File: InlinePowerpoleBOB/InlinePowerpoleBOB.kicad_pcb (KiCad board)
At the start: 2 copper layers, 65.4 x 36.8 mm, 17 parts, among them IC1 LTC4368IMS-2#PBF, Q1 DMT6002LPS-13, Q2 DMT6002LPS-13

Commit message: PCB Updates
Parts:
- added G***: LOGO, OpenSourceLogos:ohs-logo, B.Cu at (128.5, 60.5)
- J1: renamed from Input; footprint SamacSys_Parts:Anderson_powerpole_2w -> SamacSys_Parts:Anderson_powerpole_2w_90
- J2: renamed from Output; footprint SamacSys_Parts:Anderson_powerpole_2w -> SamacSys_Parts:Anderson_powerpole_2w_90
- moved J1 2.79 mm to (117.1, 55.2)
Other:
- board text added: "Inline Poerpole protection by Gareth Blades M7GRB Based on the design by Bernard McIntosh GM4WZG featured in RadCom September 2021"
- board text added: "Input"
- board text added: "Output"
- board text added: "https://bit.ly/2YlUq2V"

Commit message: Fixed PCB text
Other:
- board text added: "Inline Powerpole protection by Gareth Blades M7GRB Based on the design by Bernard McIntosh GM4WZG featured in RadCom September 2021"
- board text removed: "Inline Poerpole protection by Gareth Blades M7GRB Based on the design by Bernard McIntosh GM4WZG featured in RadCom September 2021"

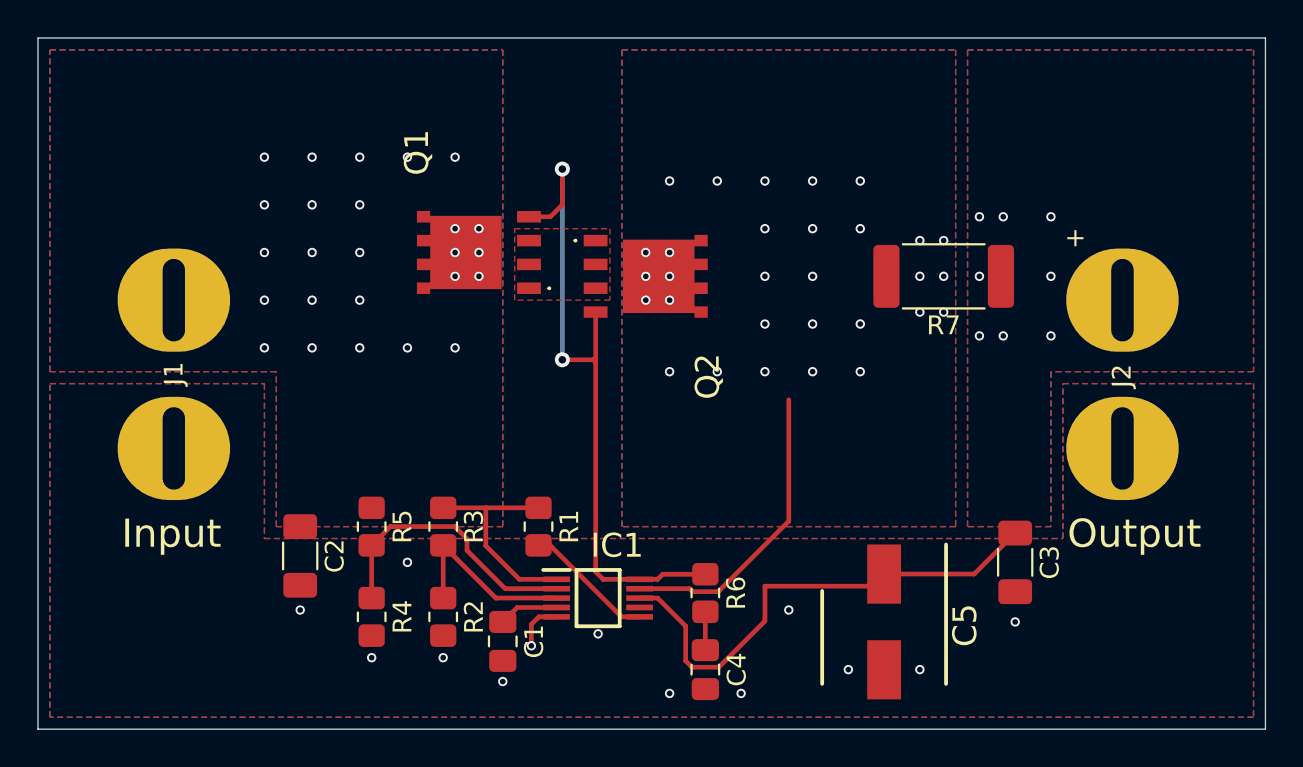
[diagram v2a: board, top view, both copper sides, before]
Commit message: Removed over current feature
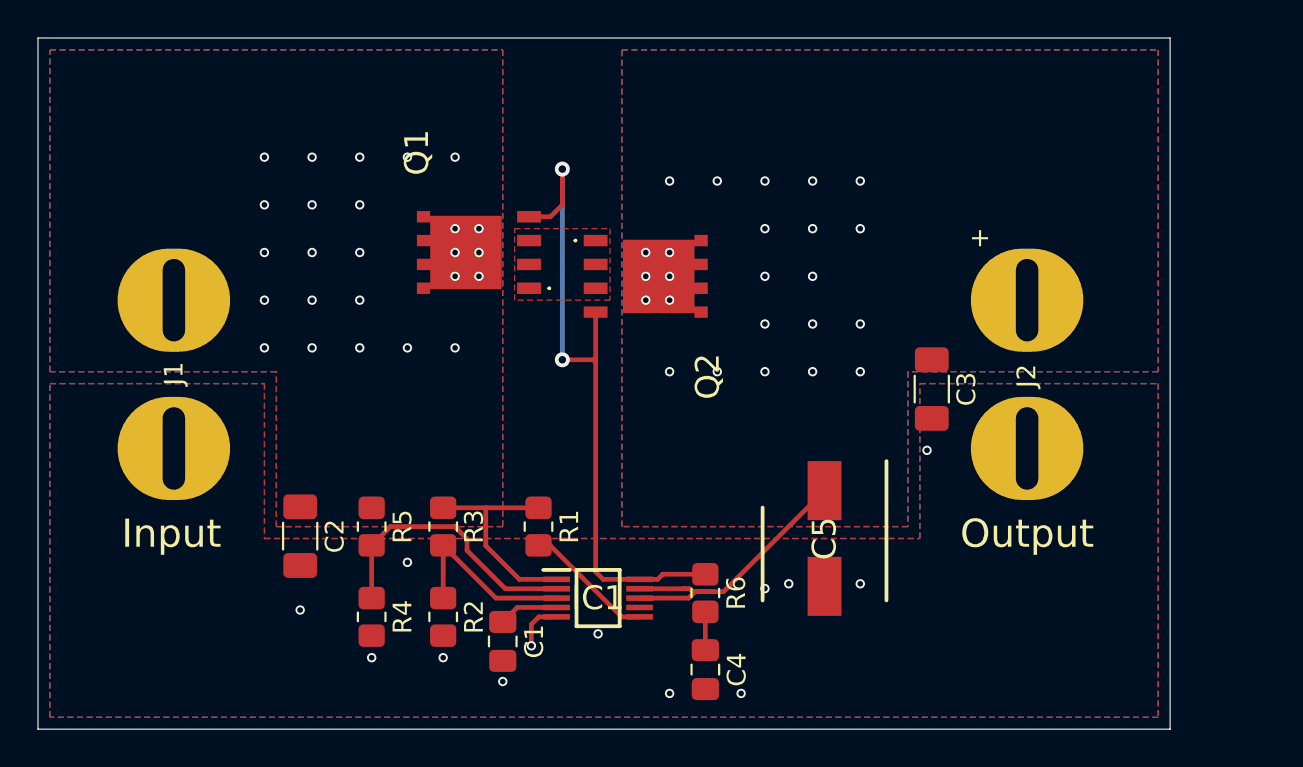
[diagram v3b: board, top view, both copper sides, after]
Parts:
- removed R7: 0R002, Resistor_SMD:R_2512_6332Metric_Pad1.40x3.35mm_HandSolder
- moved C3 10.2 mm to (157.5, 60.0)
- moved C5 5.46 mm to (151.8, 67.9)
- moved J2 5.08 mm to (162.6, 55.2)
- moved C2 1.05 mm to (123.8, 67.8)
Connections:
- IC1 pad 9: Net-(IC1-Pad9) -> Net-(C3-Pad1)
- Q2 pad 3: Net-(IC1-Pad9) -> Net-(C3-Pad1)
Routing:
- net Net-(IC1-Pad9): track 16.0 -> 0.00 mm, vias 30 -> 0
- net Net-(C3-Pad1): track 26.7 -> 16.2 mm, vias 8 -> 24
- removed copper zone on B.Cu, net Net-(IC1-Pad9)
- removed copper zone on F.Cu, net Net-(IC1-Pad9)
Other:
- board size 65.4 x 36.8 mm -> 60.3 x 36.8 mm
- board text added: "V1.1"

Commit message: V1.1 update
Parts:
- removed R4: 62K, Resistor_SMD:R_0805_2012Metric_Pad1.20x1.40mm_HandSolder
- added D1: 15V, Diode_SMD:D_0805_2012Metric, F.Cu at (127.6, 72.2)
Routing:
- net Net-(C3-Pad1): track 16.2 -> 42.8 mm
- net Net-(C2-Pad1): track 11.9 -> 35.2 mm
